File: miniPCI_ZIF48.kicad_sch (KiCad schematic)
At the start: 18 parts

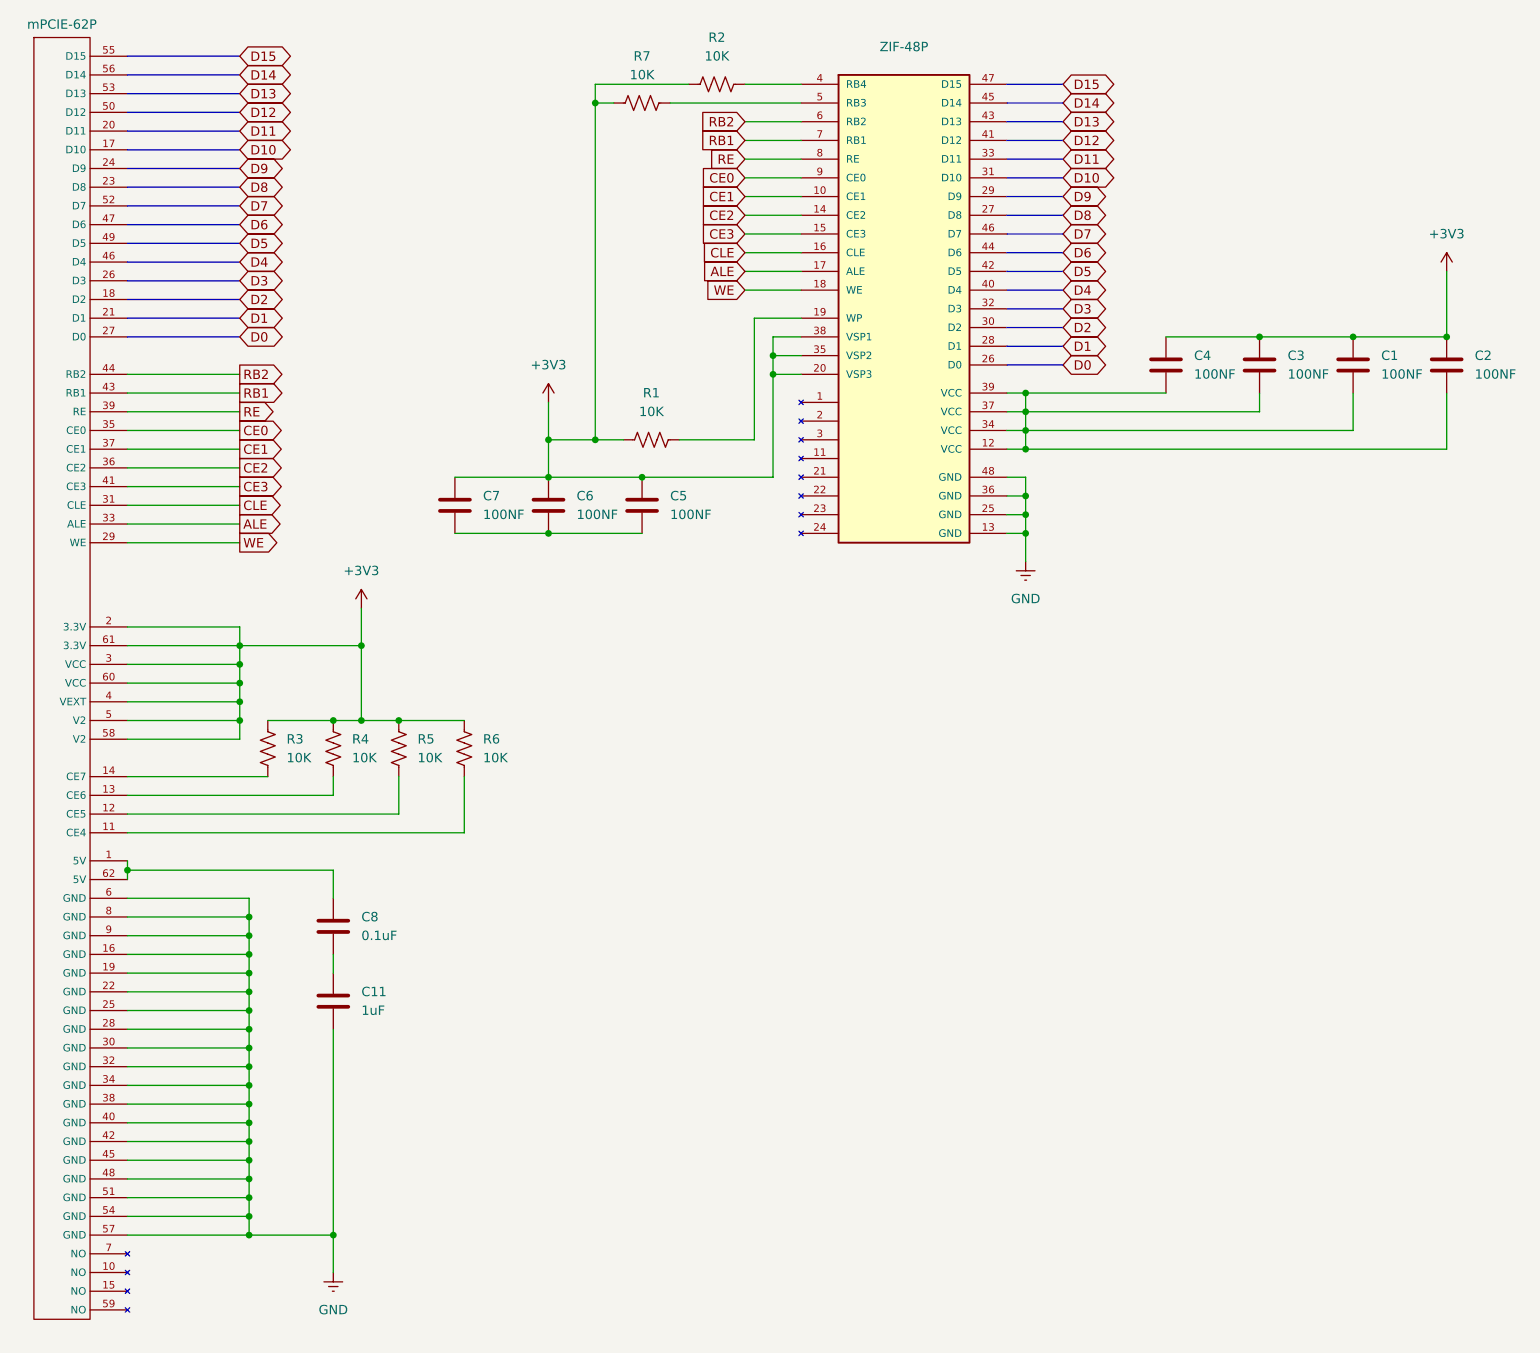
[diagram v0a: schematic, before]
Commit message: Fix ZIF pinout to exactly similiar to NAND schematic
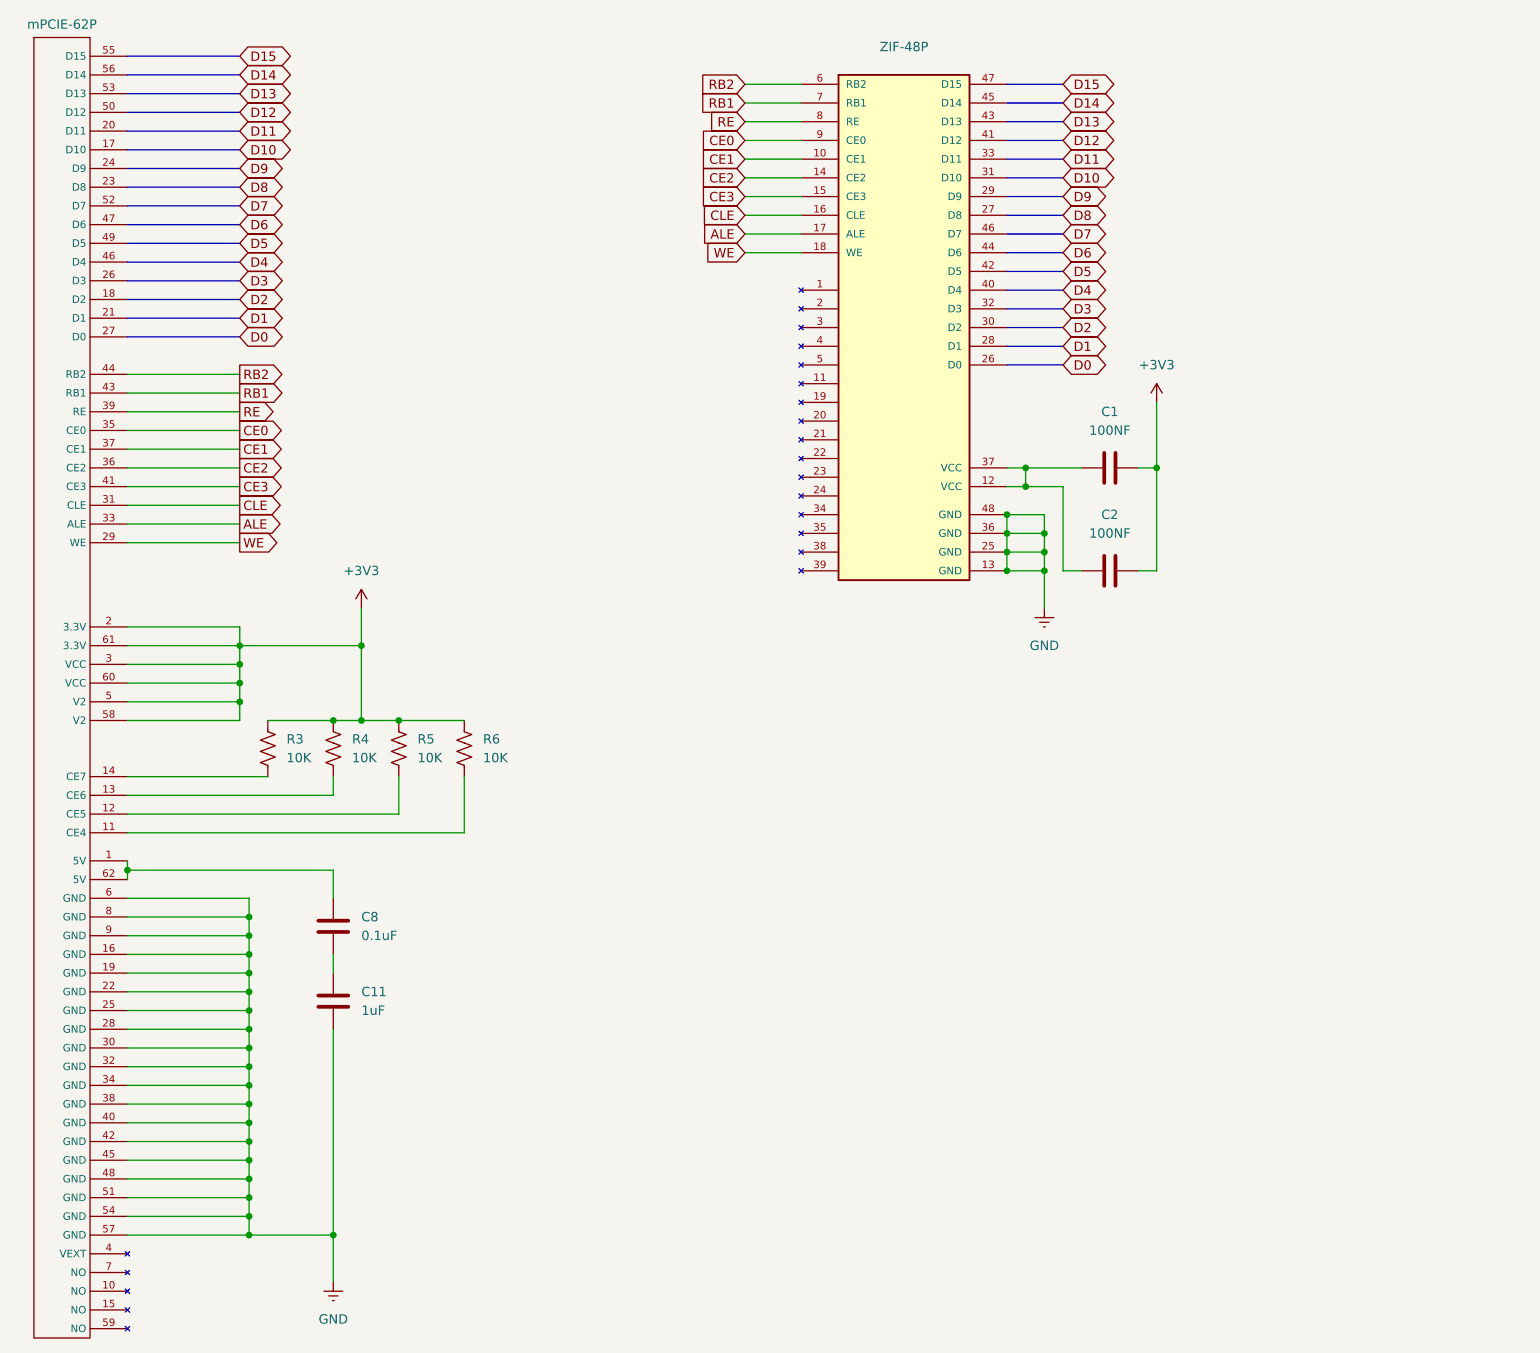
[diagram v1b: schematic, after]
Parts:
- removed C3, C4, C5, C6, C7: 100NF, Capacitor_SMD:C_1206_3216Metric, symbol Device:C
- removed R1, R2, R7: 10K, symbol Device:R_US
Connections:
- net +3V3: now also C1.1, C2.1; no longer C1.2, C2.2, ZIF-48P.20 (VSP3), ZIF-48P.35 (VSP2), ZIF-48P.38 (VSP1), mPCIE-62P.4 (VEXT)
- new net: C1.2, C2.2, ZIF-48P.12 (VCC), ZIF-48P.37 (VCC)
- now unconnected: ZIF-48P.34 (VCC), ZIF-48P.39 (VCC)
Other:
- moved on the sheet: C1, C2

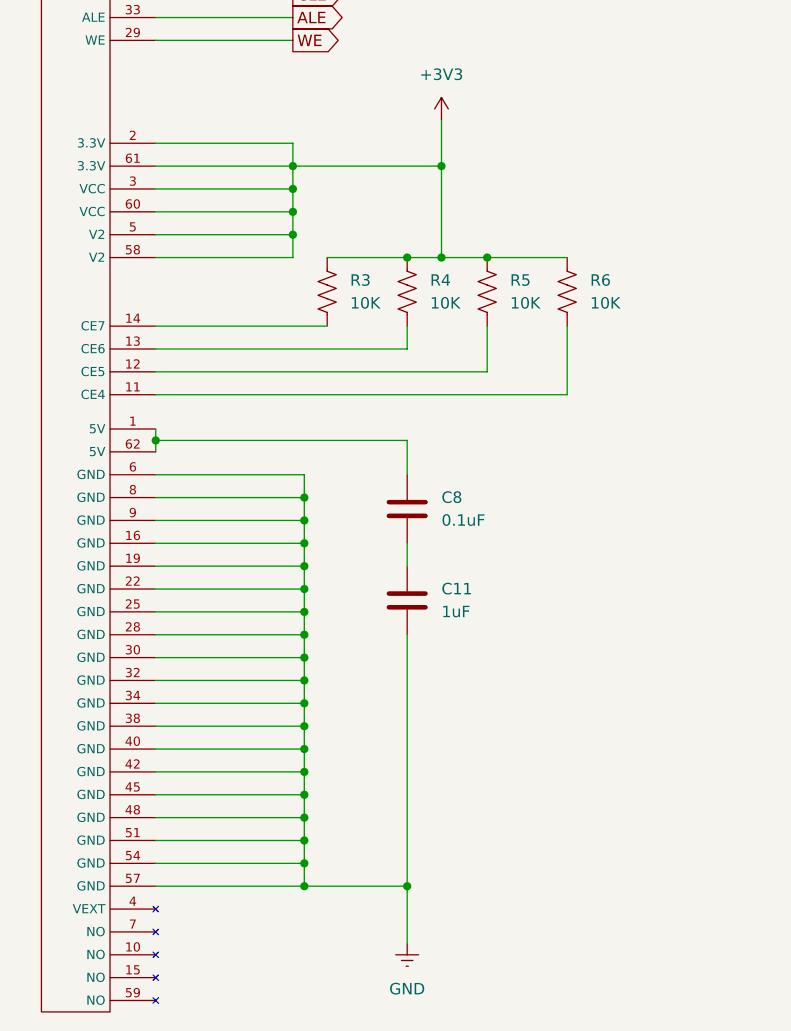
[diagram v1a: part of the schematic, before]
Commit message: remove unused pins on mPCIE
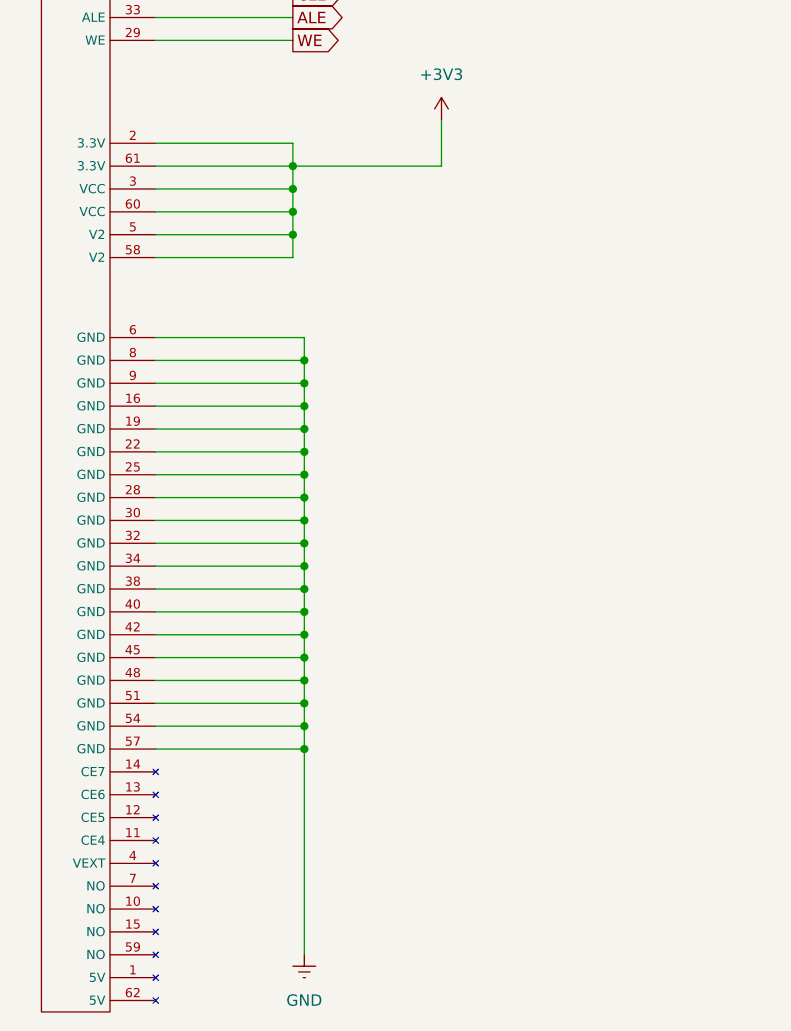
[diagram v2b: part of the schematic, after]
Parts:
- removed C11: 1uF, Capacitor_SMD:C_1206_3216Metric, symbol Device:C
- removed C8: 0.1uF, Capacitor_SMD:C_1206_3216Metric, symbol Device:C
- removed R3, R4, R5, R6: 10K, symbol Device:R_US
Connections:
- net at mPCIE-62P.1 (5V): no longer mPCIE-62P.62 (5V)
